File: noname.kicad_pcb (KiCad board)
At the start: 4 copper layers, 100 x 100 mm, 198 parts, among them J0 Conn_01x10_Female, J1 Conn_01x10_Female, J2 Conn_01x10_Female, J3 Conn_01x10_Female, U0 ATmega1284P-AU, U1 CH340B, U2 ICSP, Y0 16MHz

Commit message: Change footprint
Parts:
- mouse-bite-2mm-slot (x72): footprint analogPidBoard:mouse-bite-2mm-slot -> panelSystemChip:mouse-bite-2mm-slot

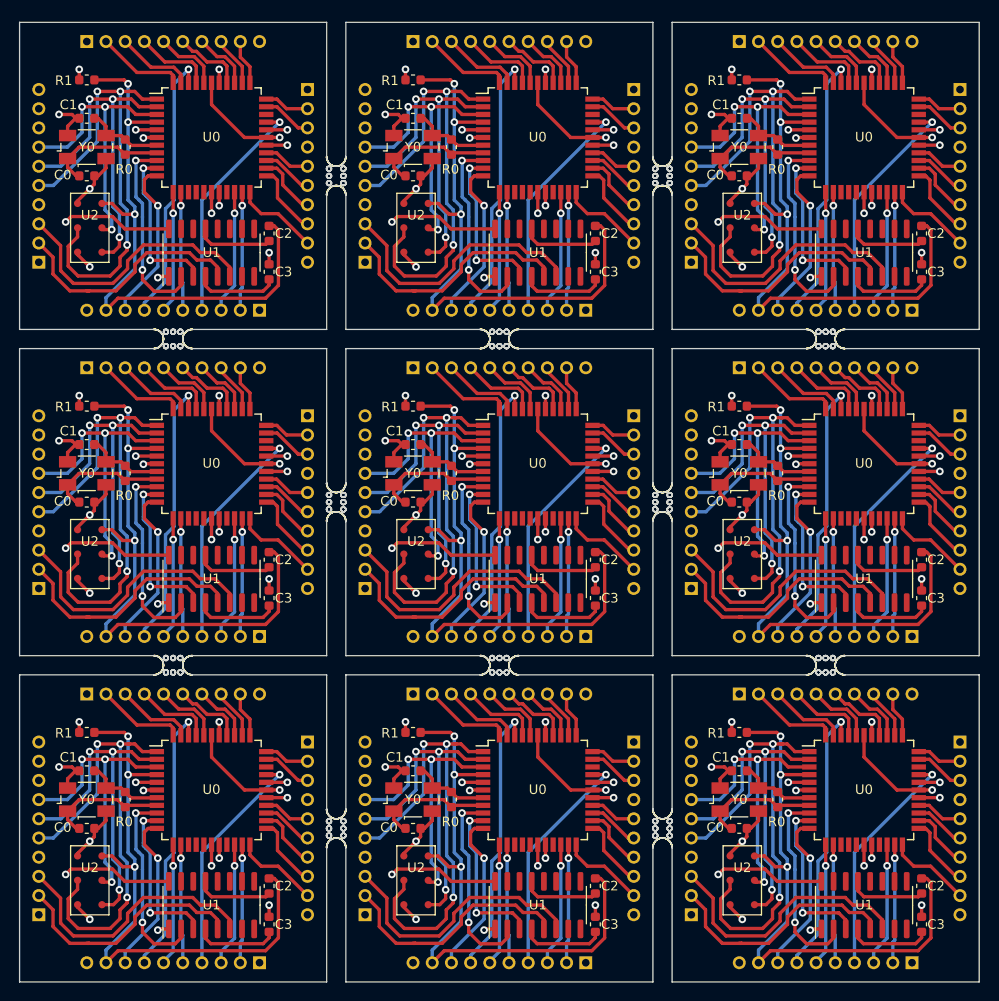
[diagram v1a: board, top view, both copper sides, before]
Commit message: Add BOM file and CPL file
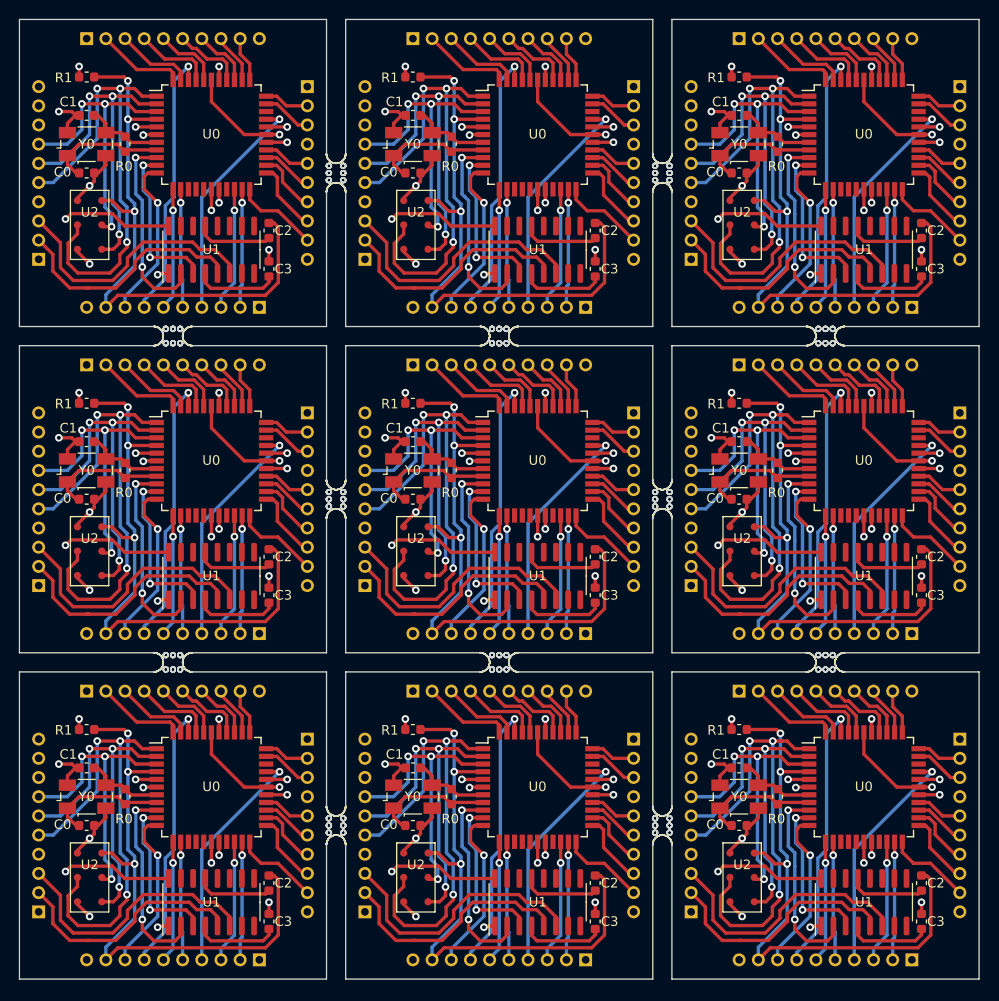
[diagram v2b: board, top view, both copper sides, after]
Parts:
- moved mouse-bite-2mm-slot 0.30 mm to (113.0, 141.0) (x3)
- moved C0 0.30 mm to (155.0, 141.0)
- moved C0 0.30 mm to (121.0, 141.0)
- moved C0 0.30 mm to (87.0, 141.0)
- moved C1 0.30 mm to (155.0, 135.0)
- moved C1 0.30 mm to (121.0, 135.0)
- moved C1 0.30 mm to (87.0, 135.0)
- moved C2 0.30 mm to (174.0, 147.0)
- moved C2 0.30 mm to (140.0, 147.0)
- moved C2 0.30 mm to (106.0, 147.0)
- moved C3 0.30 mm to (174.0, 151.0)
- moved C3 0.30 mm to (140.0, 151.0)
- moved C3 0.30 mm to (106.0, 151.0)
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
